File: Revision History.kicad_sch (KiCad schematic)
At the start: 0 parts

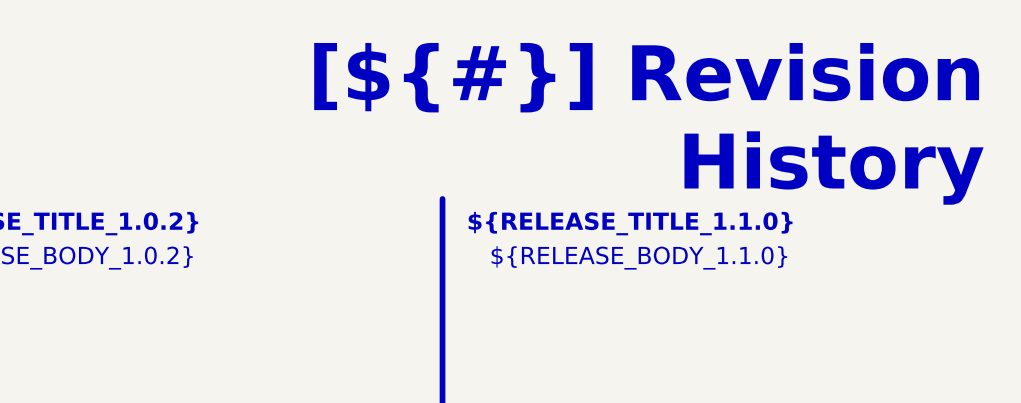
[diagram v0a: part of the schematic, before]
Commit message: Reworked sheet titles
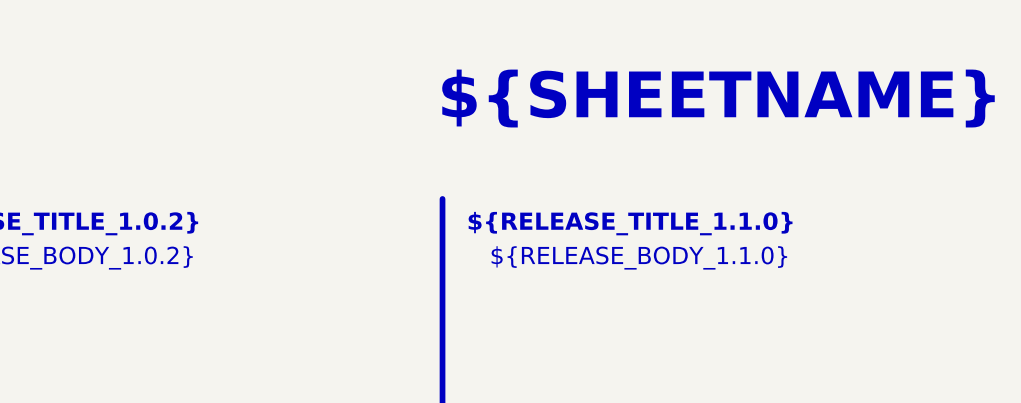
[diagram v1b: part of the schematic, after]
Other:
- title: Revision History -> ${SHEETNAME}
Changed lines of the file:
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@@
 	(paper "A4")
 	(title_block
-		(title "Revision History")
+		(title "${SHEETNAME}")
 		(date "2025-01-12")
 		(rev "${REVISION}")
@@
 			)
 			(justify left top)
-		)
-	)
-	(text_box "[${#}] ${TITLE}"
-		(exclude_from_sim no)
-		(at 177.8 16.51 0)
-		(size 104.14 12.7)
-		(margins 4.4999 4.4999 4.4999 4.4999)
-		(stroke
-			(width -0.0001)
-			(type solid)
-		)
-		(fill
-			(type none)
-		)
-		(effects
-			(font
-				(face "Times New Roman")
-				(size 6.096 6.096)
-				(thickness 1.2)
-				(bold yes)
-				(color 0 0 194 1)
-			)
-			(justify right)
 		)
 	)
@@
 		)
 	)
+	(text_box "${SHEETNAME}"
+		(exclude_from_sim no)
+		(at 223.52 15.24 0)
+		(size 58.42 10.16)
+		(margins 2.54 1.27 2.54 1.27)
+		(stroke
+			(width -0.0001)
+			(type solid)
+		)
+		(fill
+			(type none)
+		)
+		(effects
+			(font
+				(face "Times New Roman")
+				(size 5.08 5.08)
+				(thickness 1.2)
+				(bold yes)
+				(color 0 0 194 1)
+			)
+			(justify right)
+		)
+	)

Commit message: Added PCB
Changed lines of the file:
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@@
 	(title_block
 		(title "${SHEETNAME}")
-		(date "2025-01-12")
+		(date "2025-07-04")
 		(rev "${REVISION}")
 		(company "${COMPANY}")
@@
 		(at 223.52 15.24 0)
 		(size 58.42 10.16)
-		(margins 2.54 1.27 2.54 1.27)
+		(margins 1.27 1.27 1.27 1.27)
 		(stroke
 			(width -0.0001)
